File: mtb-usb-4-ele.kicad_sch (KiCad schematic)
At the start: 73 parts, among them J1 USB_C_Receptacle_USB2.0, J2 PROG/DEBUG, J3 Conn_01x06, J4 RJ12, J5 RJ12, J6 Screw_Terminal_01x02, J7 Screw_Terminal_01x02, J8 Conn_01x02, U1 STM32F103C8Tx, U2 AMS1117-3.3, U3 ADM2483xRW, U4 ADUM1250, U6 LM78M05_TO252, U7 INA219AxDCN, Y1 8 MHz

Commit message: Add green LED, add JLCPCB_IGNORE.
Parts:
- D1: LCSC (none) -> C2297
- H1, H2, H3, J2, J3, J4, J5, J6, J7, J8, JP1, JP2, JP3, JP4, JP5, JP6, PS1, TP1, TP2, TP3, TP4, TP5, TP6, TP7: JLCPCB_IGNORE (none) -> true
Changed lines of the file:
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@@
+      (effects (font (size 1.27 1.27)) hide)
+    )
+    (property "JLCPCB_IGNORE" "true" (id 4) (at 270.51 25.4 0)
       (effects (font (size 1.27 1.27)) hide)
     )
@@
       (effects (font (size 1.27 1.27)) hide)
     )
-    (property "JLCPCB_IGNORE" "" (id 4) (at 247.65 25.4 90)
+    (property "JLCPCB_IGNORE" "true" (id 4) (at 247.65 25.4 90)
       (effects (font (size 1.27 1.27)) hide)
     )
@@
       (effects (font (size 1.27 1.27)) hide)
     )
+    (property "JLCPCB_IGNORE" "true" (id 4) (at 102.87 119.38 0)
+      (effects (font (size 1.27 1.27)) hide)
+    )
     (pin "1")
     (pin "2")
@@
     )
     (property "Datasheet" "~" (id 3) (at 120.65 116.84 0)
+      (effects (font (size 1.27 1.27)) hide)
+    )
+    (property "JLCPCB_IGNORE" "true" (id 4) (at 120.65 116.84 0)
       (effects (font (size 1.27 1.27)) hide)
     )
@@
       (effects (font (size 1.27 1.27)) hide)
     )
+    (property "JLCPCB_IGNORE" "true" (id 4) (at 128.27 78.74 0)
+      (effects (font (size 1.27 1.27)) hide)
+    )
     (pin "1")
     (pin "2")
@@
     )
     (property "Datasheet" "~" (id 3) (at 273.05 52.07 0)
+      (effects (font (size 1.27 1.27)) hide)
+    )
+    (property "JLCPCB_IGNORE" "true" (id 4) (at 273.05 52.07 0)
       (effects (font (size 1.27 1.27)) hide)
     )
@@
     )
     (property "Datasheet" "~" (id 3) (at 270.51 129.54 0)
+      (effects (font (size 1.27 1.27)) hide)
+    )
+    (property "JLCPCB_IGNORE" "true" (id 4) (at 270.51 129.54 0)
       (effects (font (size 1.27 1.27)) hide)
     )
@@
       (effects (font (size 1.27 1.27)) hide)
     )
+    (property "JLCPCB_IGNORE" "true" (id 4) (at 201.93 149.86 0)
+      (effects (font (size 1.27 1.27)) hide)
+    )
     (pin "1")
     (pin "2")
@@
       (effects (font (size 1.27 1.27)) hide)
     )
+    (property "JLCPCB_IGNORE" "true" (id 4) (at 139.7 125.73 0)
+      (effects (font (size 1.27 1.27)) hide)
+    )
     (pin "1")
     (pin "2")
@@
     )
     (property "Datasheet" "~" (id 3) (at 135.89 146.05 0)
+      (effects (font (size 1.27 1.27)) hide)
+    )
+    (property "JLCPCB_IGNORE" "true" (id 4) (at 135.89 146.05 0)
       (effects (font (size 1.27 1.27)) hide)
     )
@@
       (effects (font (size 1.27 1.27)) (justify left) hide)
     )
+    (property "JLCPCB_IGNORE" "true" (id 4) (at 187.96 152.4 0)
+      (effects (font (size 1.27 1.27)) hide)
+    )
     (pin "1")
     (pin "2")
@@
       (effects (font (size 1.27 1.27)) hide)
     )
+    (property "JLCPCB_IGNORE" "true" (id 4) (at 111.76 148.59 0)
+      (effects (font (size 1.27 1.27)) hide)
+    )
     (pin "1")
     (pin "2")
@@
       (effects (font (size 1.27 1.27)) hide)
     )
+    (property "LCSC" "C2297" (id 4) (at 100.33 43.18 0)
+      (effects (font (size 1.27 1.27)) hide)
+    )
     (pin "1")
     (pin "2")
@@
       (effects (font (size 1.27 1.27)) hide)
     )
+    (property "JLCPCB_IGNORE" "true" (id 4) (at 265.43 139.7 0)
+      (effects (font (size 1.27 1.27)) hide)
+    )
     (pin "1")
   )
@@
     )
     (property "Datasheet" "~" (id 3) (at 33.02 116.84 0)
+      (effects (font (size 1.27 1.27)) hide)
+    )
+    (property "JLCPCB_IGNORE" "true" (id 4) (at 27.94 116.84 0)
       (effects (font (size 1.27 1.27)) hide)
     )
@@
       (effects (font (size 1.27 1.27)) hide)
     )
+    (property "JLCPCB_IGNORE" "true" (id 4) (at 161.29 39.37 0)
+      (effects (font (size 1.27 1.27)) hide)
+    )
     (pin "1")
   )
@@
       (effects (font (size 1.27 1.27)) hide)
     )
+    (property "JLCPCB_IGNORE" "true" (id 4) (at 161.29 44.45 0)
+      (effects (font (size 1.27 1.27)) hide)
+    )
     (pin "1")
   )
@@
       (effects (font (size 1.27 1.27)) hide)
     )
+    (property "JLCPCB_IGNORE" "true" (id 4) (at 161.29 49.53 0)
+      (effects (font (size 1.27 1.27)) hide)
+    )
     (pin "1")
   )
@@
       (effects (font (size 1.27 1.27)) hide)
     )
+    (property "JLCPCB_IGNORE" "true" (id 4) (at 156.21 95.25 0)
+      (effects (font (size 1.27 1.27)) hide)
+    )
     (pin "1")
   )
@@
     )
     (property "Datasheet" "~" (id 3) (at 160.02 90.17 0)
+      (effects (font (size 1.27 1.27)) hide)
+    )
+    (property "JLCPCB_IGNORE" "true" (id 4) (at 165.1 90.17 0)
       (effects (font (size 1.27 1.27)) hide)
     )
@@
     )
     (property "Datasheet" "~" (id 3) (at 100.33 85.09 0)
+      (effects (font (size 1.27 1.27)) hide)
+    )
+    (property "JLCPCB_IGNORE" "true" (id 4) (at 100.33 85.09 0)
       (effects (font (size 1.27 1.27)) hide)
     )
@@
       (effects (font (size 1.27 1.27)) hide)
     )
+    (property "JLCPCB_IGNORE" "true" (id 4) (at 214.63 124.46 0)
+      (effects (font (size 1.27 1.27)) hide)
+    )
     (pin "1")
     (pin "2")
@@
       (effects (font (size 1.27 1.27)) hide)
     )
+    (property "JLCPCB_IGNORE" "true" (id 4) (at 161.29 180.34 0)
+      (effects (font (size 1.27 1.27)) hide)
+    )
     (pin "1")
   )
@@
       (effects (font (size 1.27 1.27)) hide)
     )
+    (property "JLCPCB_IGNORE" "true" (id 4) (at 156.21 180.34 0)
+      (effects (font (size 1.27 1.27)) hide)
+    )
     (pin "1")
   )
@@
       (effects (font (size 1.27 1.27)) hide)
     )
+    (property "JLCPCB_IGNORE" "true" (id 4) (at 158.75 186.69 0)
+      (effects (font (size 1.27 1.27)) hide)
+    )

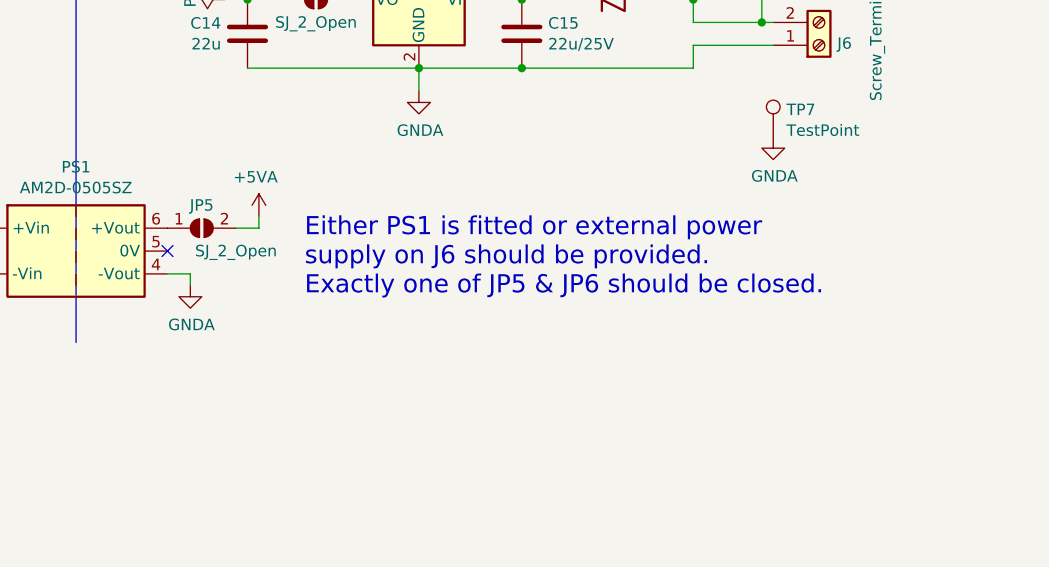
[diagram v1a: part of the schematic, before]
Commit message: AM2D-0505: allow both SZ&DZ variants: add solderjumper.
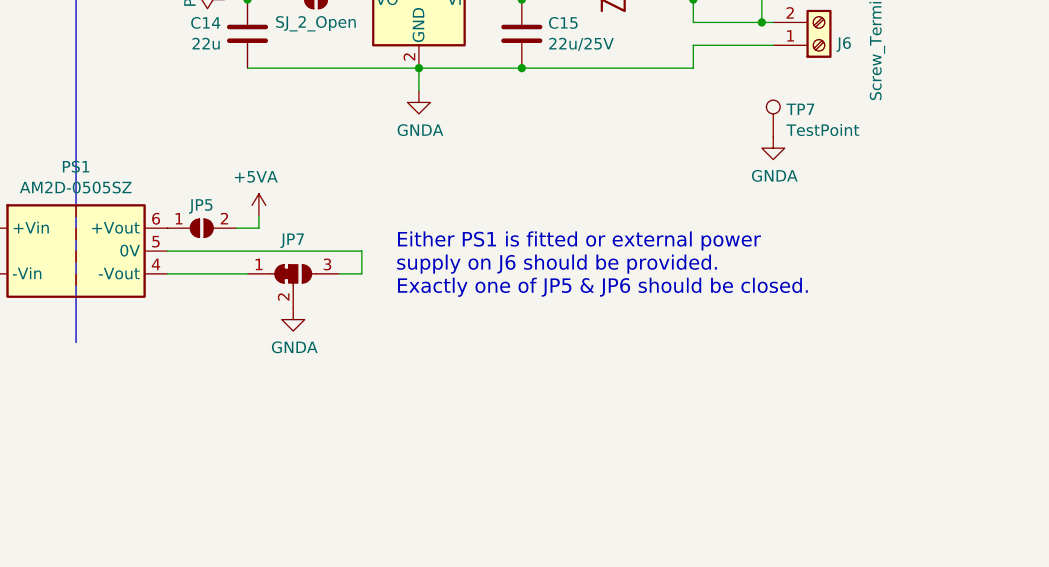
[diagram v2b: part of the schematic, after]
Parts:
- added JP7: SJ3_Bridged12, Jumper:SolderJumper-3_P1.3mm_Bridged12_RoundedPad1.0x1.5mm_NumberLabels, symbol Jumper:SolderJumper_3_Bridged12
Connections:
- net GNDA: now also JP7.2 (C); no longer PS1.4 (-Vout)
- net at PS1.5 (0V): now also JP7.3 (B)
- new net: JP7.1 (A), PS1.4 (-Vout)
- no-connect marks 29 -> 28
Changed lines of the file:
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@@
   (no_connect (at 156.21 182.88))
   (no_connect (at 54.61 167.64))
-  (no_connect (at 198.12 152.4))
   (no_connect (at 86.36 82.55))
   (no_connect (at 130.81 140.97))
   (no_connect (at 53.34 74.93))
+  (wire (pts (xy 198.12 152.4) (xy 219.71 152.4))
+    (stroke (width 0) (type default) (color 0 0 0 0))
+  )
   (wire (pts (xy 73.66 29.21) (xy 73.66 31.75))
     (stroke (width 0) (type default) (color 0 0 0 0))
@@
     (stroke (width 0) (type default) (color 0 0 0 0))
   )
+  (wire (pts (xy 198.12 154.94) (xy 207.01 154.94))
+    (stroke (width 0) (type default) (color 0 0 0 0))
+  )
   (wire (pts (xy 57.15 29.21) (xy 45.72 29.21))
     (stroke (width 0) (type default) (color 0 0 0 0))
@@
     (stroke (width 0) (type default) (color 0 0 0 0))
   )
+  (wire (pts (xy 219.71 154.94) (xy 217.17 154.94))
+    (stroke (width 0) (type default) (color 0 0 0 0))
+  )
   (wire (pts (xy 71.12 29.21) (xy 73.66 29.21))
     (stroke (width 0) (type default) (color 0 0 0 0))
@@
     (stroke (width 0) (type default) (color 0 0 0 0))
   )
-  (wire (pts (xy 198.12 154.94) (xy 200.66 154.94))
+  (wire (pts (xy 54.61 154.94) (xy 69.85 154.94))
     (stroke (width 0) (type default) (color 0 0 0 0))
   )
-  (wire (pts (xy 54.61 154.94) (xy 69.85 154.94))
+  (wire (pts (xy 219.71 152.4) (xy 219.71 154.94))
     (stroke (width 0) (type default) (color 0 0 0 0))
   )
@@
     (stroke (width 0) (type default) (color 0 0 0 0))
   )
-  (wire (pts (xy 200.66 154.94) (xy 200.66 156.21))
-    (stroke (width 0) (type default) (color 0 0 0 0))
-  )
   (wire (pts (xy 66.04 107.95) (xy 68.58 107.95))
     (stroke (width 0) (type default) (color 0 0 0 0))
@@
   )
   (text "Either PS1 is fitted or external power\nsupply on J6 should be provided.\nExactly one of JP5 & JP6 should be closed."
-    (at 213.36 157.48 0)
-    (effects (font (size 2.0066 2.0066)) (justify left bottom))
+    (at 223.52 157.48 0)
+    (effects (font (size 1.6 1.6)) (justify left bottom))
   )
   (text "250 mA max (bus shorted)" (at 194.31 22.86 0)
@@
     (in_bom yes) (on_board yes)
     (property "Reference" "JP5" (id 0) (at 201.93 147.32 0))
-    (property "Value" "SJ_2_Open" (id 1) (at 205.74 152.4 0))
+    (property "Value" "SJ_2_Open" (id 1) (at 205.74 152.4 0)
+      (effects (font (size 1.27 1.27)) hide)
+    )
     (property "Footprint" "Jumper:SolderJumper-2_P1.3mm_Open_RoundedPad1.0x1.5mm" (id 2) (at 201.93 149.86 0)
       (effects (font (size 1.27 1.27)) hide)
@@
     (pin "1")
   )
-  (symbol (lib_id "power:GNDA") (at 200.66 156.21 0) (unit 1)
+  (symbol (lib_id "power:GNDA") (at 212.09 158.75 0) (unit 1)
     (in_bom yes) (on_board yes)
-    (property "Reference" "#PWR047" (id 0) (at 200.66 162.56 0)
+    (property "Reference" "#PWR047" (id 0) (at 212.09 165.1 0)
       (effects (font (size 1.27 1.27)) hide)
     )
-    (property "Value" "GNDA" (id 1) (at 200.787 160.6042 0))
-    (property "Footprint" "" (id 2) (at 200.66 156.21 0)
+    (property "Value" "GNDA" (id 1) (at 212.217 163.1442 0))
+    (property "Footprint" "" (id 2) (at 212.09 158.75 0)
       (effects (font (size 1.27 1.27)) hide)
     )
-    (property "Datasheet" "" (id 3) (at 200.66 156.21 0)
+    (property "Datasheet" "" (id 3) (at 212.09 158.75 0)
       (effects (font (size 1.27 1.27)) hide)
     )
@@
     (pin "1")
   )
+  (symbol (lib_id "Jumper:SolderJumper_3_Bridged12") (at 212.09 154.94 0) (unit 1)
+    (in_bom yes) (on_board yes)
+    (property "Reference" "JP7" (id 0) (at 212.09 151.13 0))
+    (property "Value" "SJ3_Bridged12" (id 1) (at 212.09 152.8596 0)
+      (effects (font (size 1.27 1.27)) hide)
+    )
+    (property "Footprint" "Jumper:SolderJumper-3_P1.3mm_Bridged12_RoundedPad1.0x1.5mm_NumberLabels" (id 2) (at 212.09 154.94 0)
+      (effects (font (size 1.27 1.27)) hide)
+    )
+    (property "Datasheet" "~" (id 3) (at 212.09 154.94 0)
+      (effects (font (size 1.27 1.27)) hide)
+    )
+    (pin "1")
+    (pin "2")
+    (pin "3")
+  )
   (sheet_instances
     (path "/" (page "1"))
@@
       (reference "JP6") (unit 1) (value "SJ_2_Open") (footprint "Jumper:SolderJumper-2_P1.3mm_Open_RoundedPad1.0x1.5mm")
     )
+    (path "/22ba7011-af16-481a-be60-4832e2fa49b7"
+      (reference "JP7") (unit 1) (value "SJ3_Bridged12") (footprint "Jumper:SolderJumper-3_P1.3mm_Bridged12_RoundedPad1.0x1.5mm_NumberLabels")
+    )
     (path "/00000000-0000-0000-0000-0000604008d6"

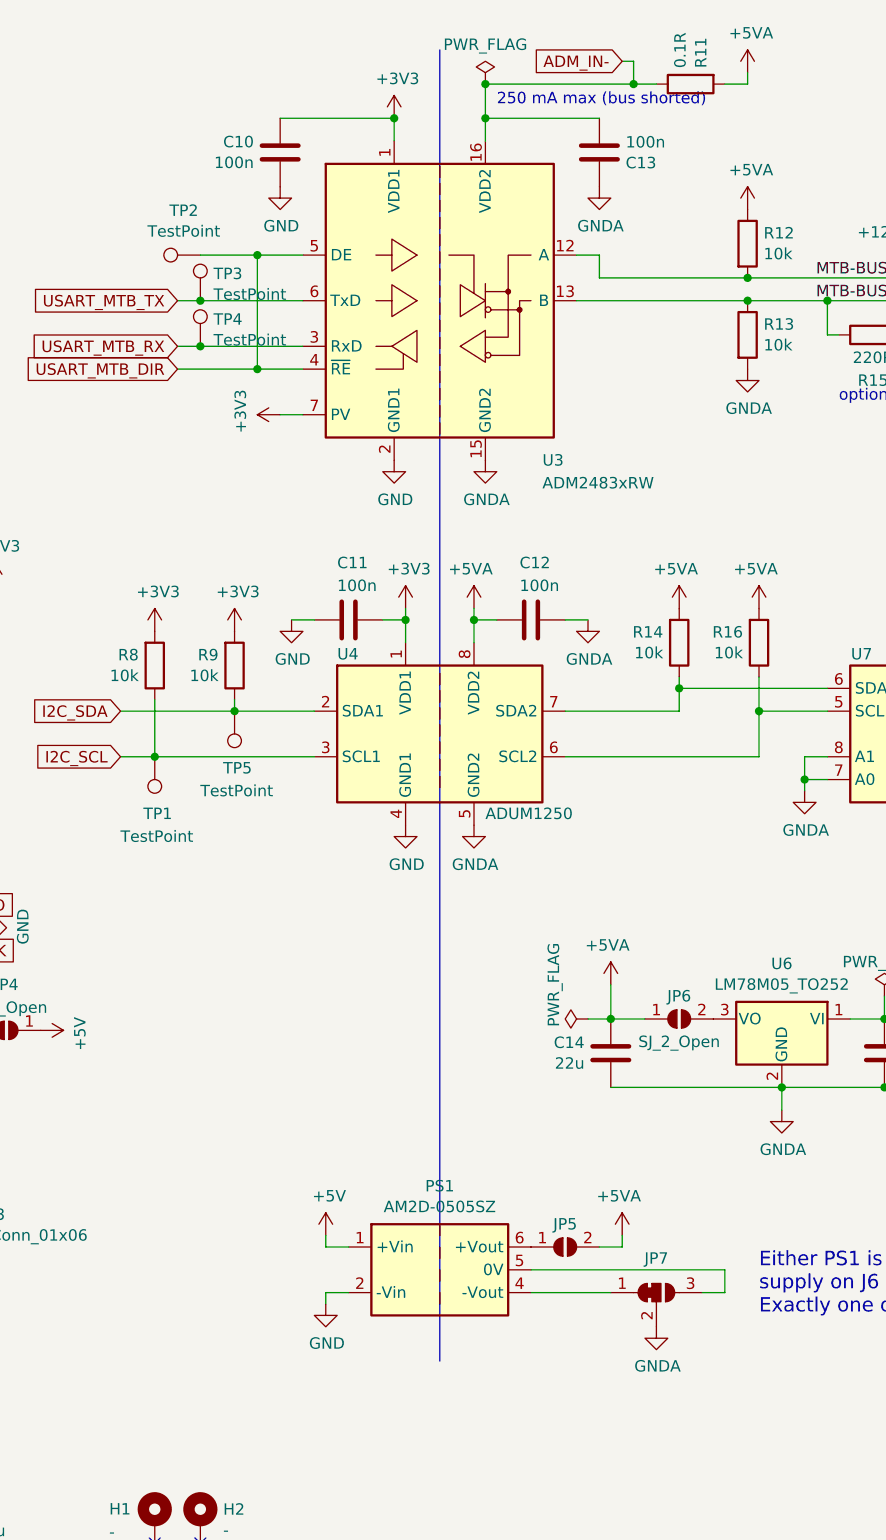
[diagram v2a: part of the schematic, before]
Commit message: Add safety resistor & capacitor between grounds.
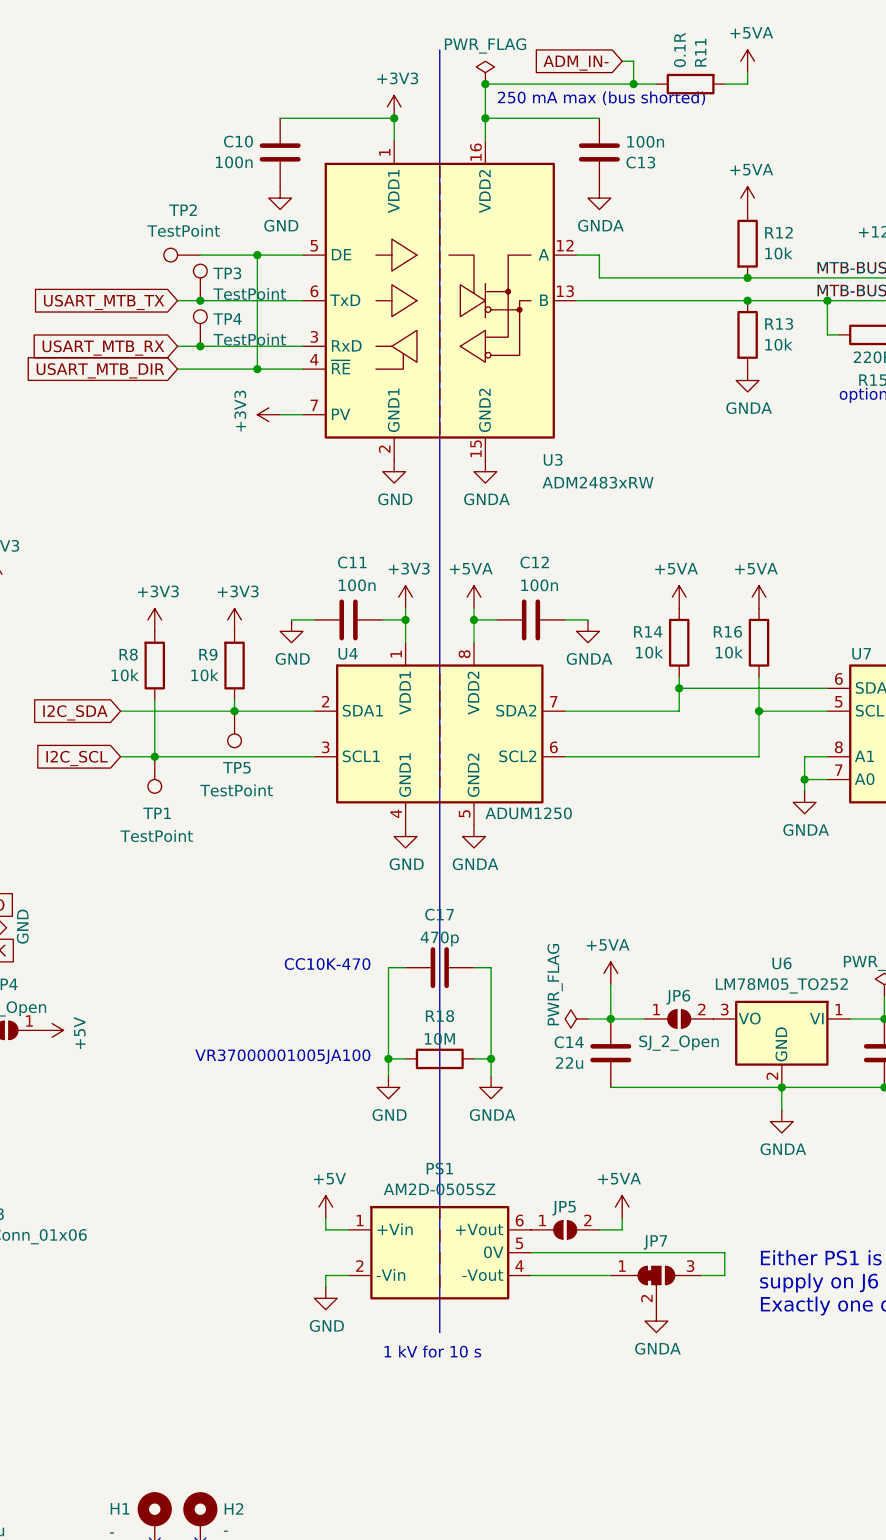
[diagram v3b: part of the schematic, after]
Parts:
- added C17: 470p, Capacitor_THT:C_Disc_D12.5mm_W5.0mm_P10.00mm, symbol Device:C
- added R18: 10M, Resistor_THT:R_Axial_DIN0207_L6.3mm_D2.5mm_P10.16mm_Horizontal, symbol Device:R
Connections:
- net GND: now also C17.1, R18.2
- net GNDA: now also C17.2, R18.1
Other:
- note added: "1 kV for 10 s"
- note added: "CC10K-470"
- note added: "VR37000001005JA100"
- moved on the sheet: JP5, JP7, PS1
